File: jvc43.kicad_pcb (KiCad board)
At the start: 6 copper layers, 101.6 x 50.8 mm, 119 parts, among them J201 8P8C_LED_Shielded, J301 8P8C_LED_Shielded, J401 USB_C_Receptacle_USB2.0, U201 LAN8810, U301 LAN8810, U401 LTC3622*DE

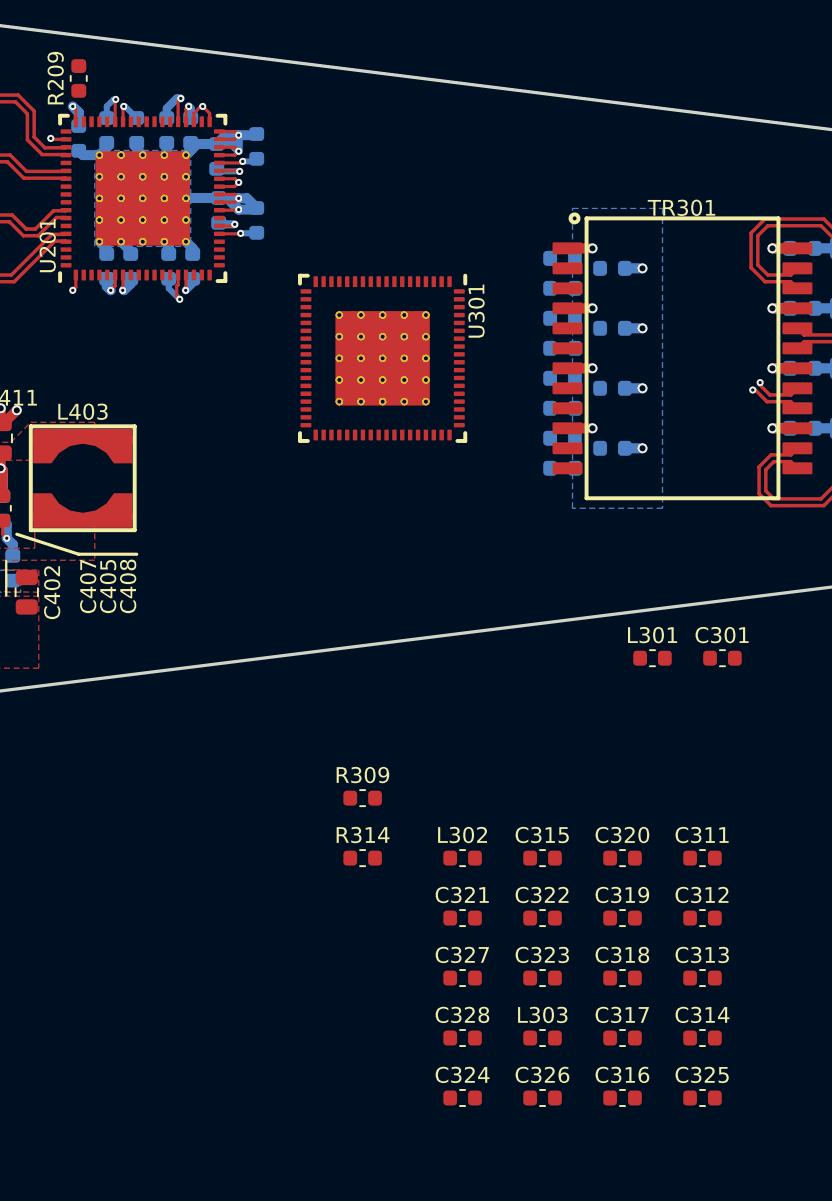
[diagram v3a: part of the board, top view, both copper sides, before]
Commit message: Routed 3/4 of the PHY2 decoupling caps, plus the PHY1-to-PHY2 data lines (but not yet the enables/clock).  Had to alter some traces and clearances down from 8 mils to 7 mils to get a couple things to fit.
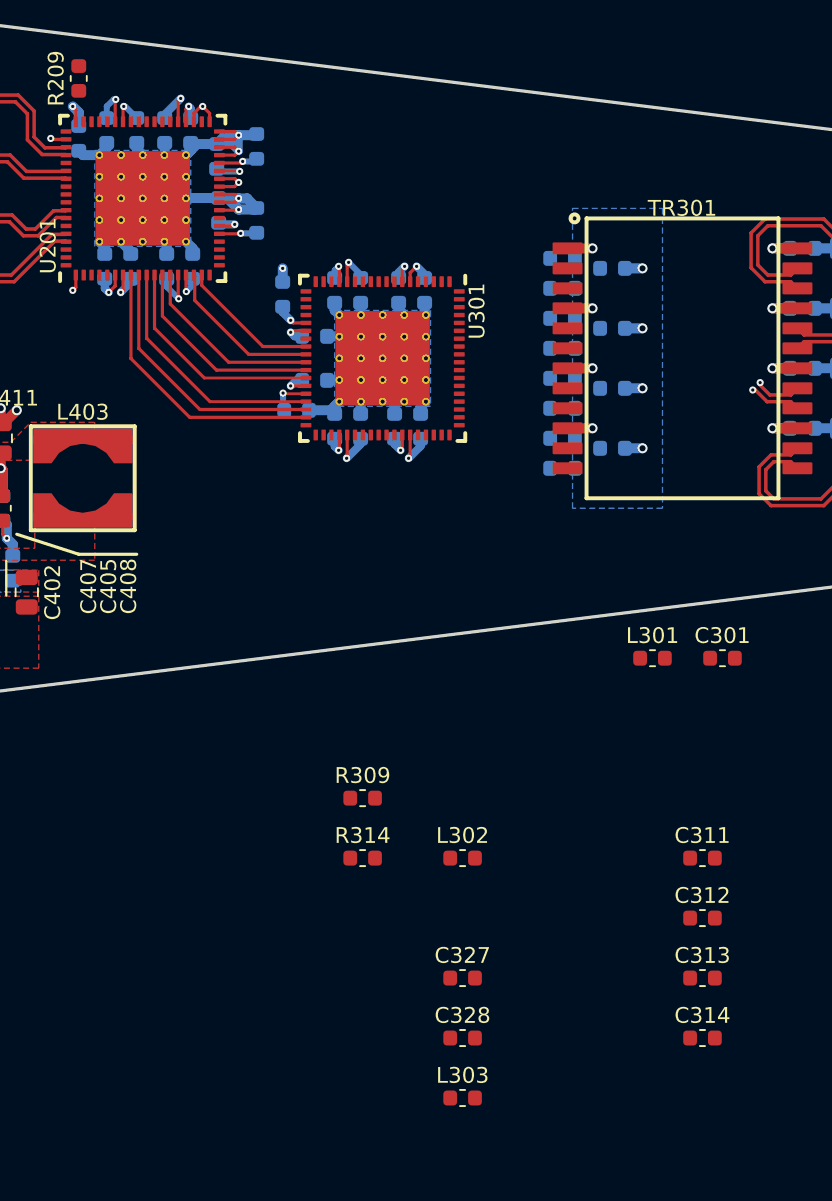
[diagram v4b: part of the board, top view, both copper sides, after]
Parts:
- C315, C316, C317, C318, C319, C320, C321, C322, C323, C324, C325, C326: moved to B.Cu
- moved C316 53.9 mm to (82.4, 46.5), turned to 270 degrees
- moved C317 51.9 mm to (77.5, 46.7), turned to 90 degrees
- moved C325 48.7 mm to (80.8, 55.1), turned to 90 degrees
- moved C324 46.6 mm to (79.5, 52.2)
- moved C326 43.7 mm to (84.6, 55.1), turned to 90 degrees
- moved C323 43.3 mm to (79.5, 49.4)
- moved C322 42.0 mm to (80.8, 46.5), turned to 270 degrees
- moved C318 41.6 mm to (78.4, 54.1)
- moved C321 40.1 mm to (84.8, 46.5), turned to 270 degrees
- moved C315 36.8 mm to (86.5, 46.5), turned to 270 degrees
- moved C319 35.4 mm to (82.4, 55.1), turned to 90 degrees
- moved C320 30.3 mm to (86.2, 55.1), turned to 90 degrees
- moved L303 6.35 mm to (88.9, 97.8)
- moved C215 0.13 mm to (66.2, 45.0)
- moved C216 0.13 mm to (70.1, 45.0)
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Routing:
- net /Ethernet1/RXD0: track 0.00 -> 18.0 mm
- net /Ethernet1/RXD1: track 0.00 -> 16.9 mm
- net /Ethernet1/RXD2: track 0.00 -> 15.8 mm
- net +2V5: track 22.2 -> 37.8 mm, vias 8 -> 14
- net /Ethernet1/RXD3: track 0.00 -> 14.3 mm
- net /Ethernet1/RXD4: track 0.00 -> 13.1 mm
- net /Ethernet1/RXD5: track 0.00 -> 12.0 mm
- net +1V2: track 24.2 -> 36.0 mm, vias 9 -> 15
- net GND: track 76.8 -> 88.0 mm, vias 35 -> 36
- net /Ethernet1/RXD6: track 0.00 -> 10.1 mm
- net /Ethernet1/RXD7: track 0.00 -> 8.89 mm
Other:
- net class CloseSig removed
- net class UghClear added: clearance 0.1778, trace_width 0.1778, via_dia 0.4572, via_drill 0.2032
- rule trace_min: 0.2032 -> 0.1778

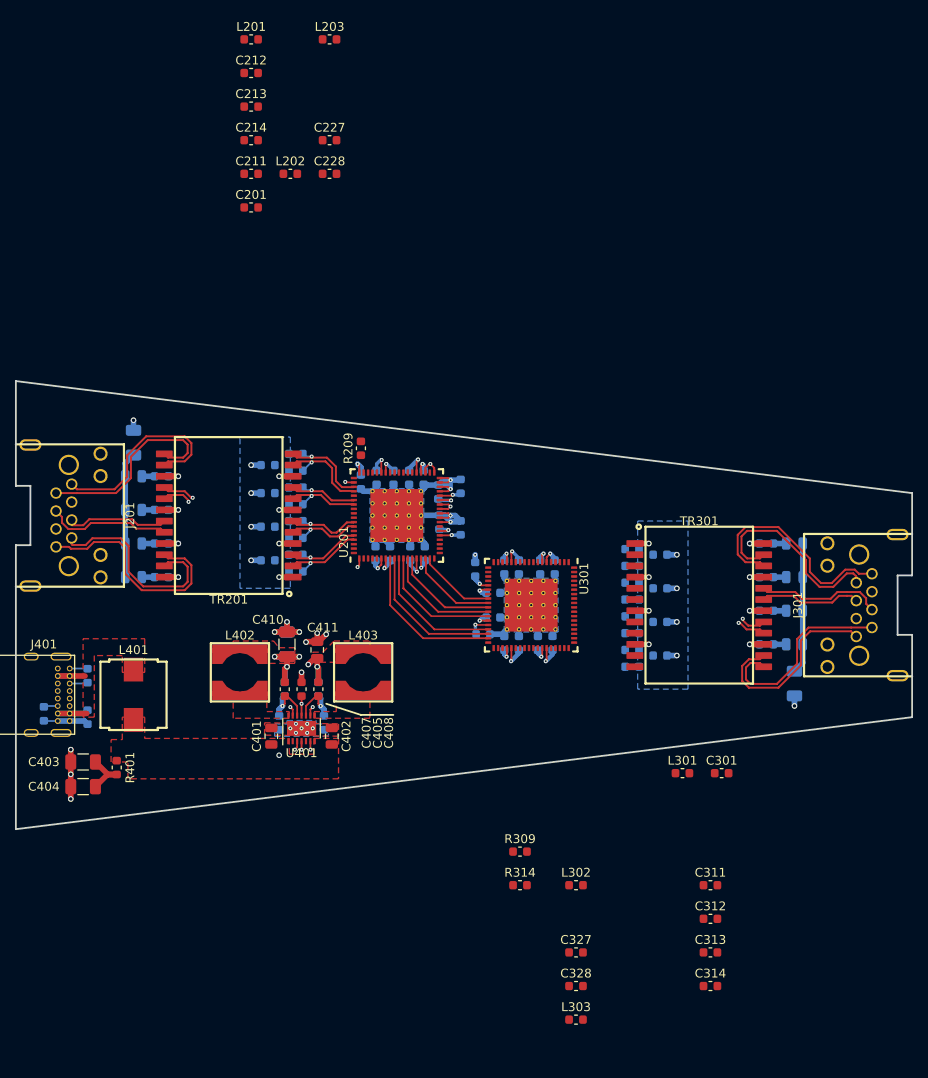
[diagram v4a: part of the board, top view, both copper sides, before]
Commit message: - Routed the PHY2-to-magnetics diff pairs - Routed all the remaining PHY2 decoupling caps, and even the chip inductors,   except for the VDD_ETH one - Spent some time swizzling rear silkscreen labels to look nice - Moved PHY1 eth_bias resistor from bottom to top, to match PHY2, and hooked   up PHY1 MDIO terminator resistor
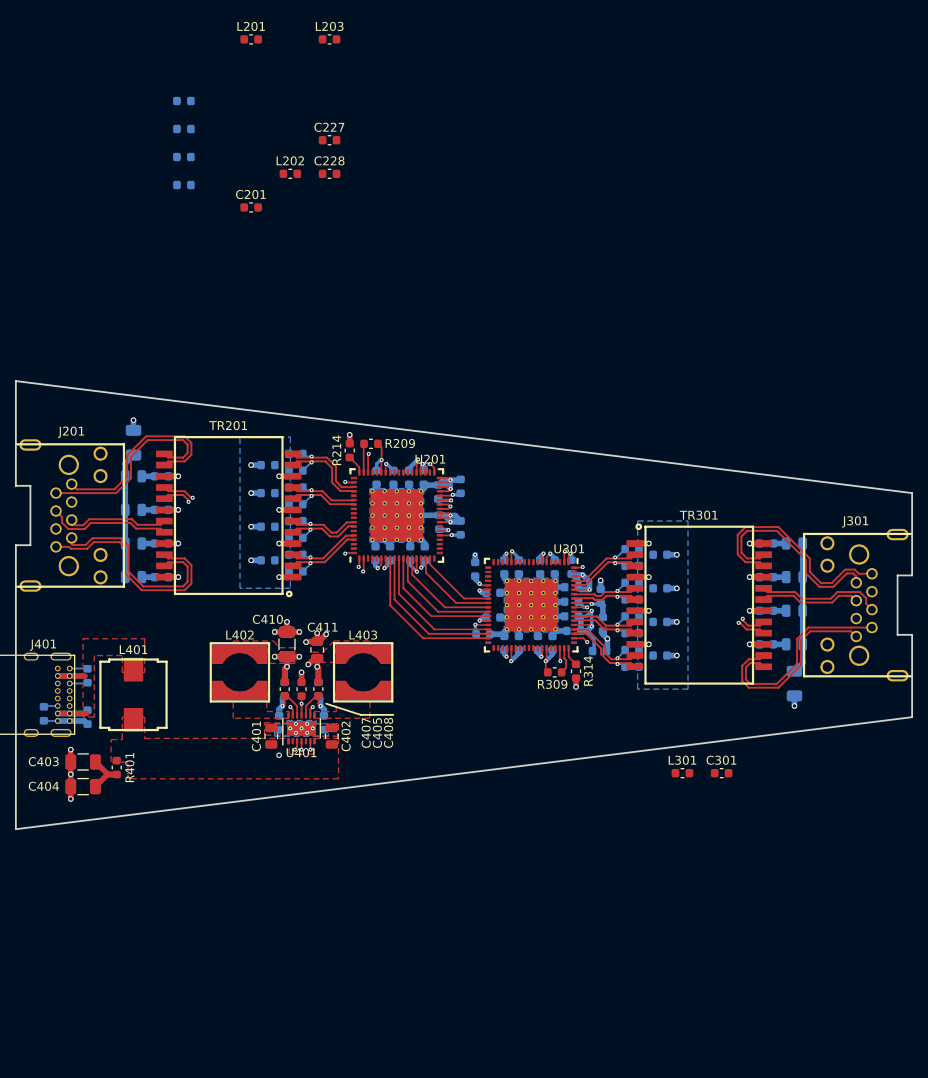
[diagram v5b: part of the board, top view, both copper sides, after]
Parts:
- C211, C212, C213, C214, C311, C312, C313, C314, C327, C328, L302, L303: moved to B.Cu
- R214: moved to F.Cu
- moved C314 50.0 mm to (88.4, 46.5), turned to 90 degrees
- moved L303 44.9 mm to (91.9, 53.0), turned to 90 degrees
- moved C313 44.3 mm to (88.4, 48.8), turned to 180 degrees
- moved C328 44.3 mm to (91.7, 49.8), turned to 90 degrees
- moved C327 39.8 mm to (88.4, 50.4), turned to 180 degrees
- moved C312 37.7 mm to (88.4, 52.1), turned to 180 degrees
- moved C311 32.7 mm to (88.6, 53.7), turned to 180 degrees
- moved L302 26.7 mm to (91.6, 56.0), turned to 180 degrees
- moved R314 25.1 mm to (88.9, 58.3), turned to 270 degrees
- moved R309 20.7 mm to (86.5, 58.4), turned to 180 degrees
- moved C211 11.2 mm to (44.5, -6.35)
- moved C212 9.92 mm to (44.5, -3.17)
- moved C213 9.52 mm to (44.5, 0.00)
- moved C214 9.16 mm to (44.5, 3.17)
- moved R214 3.78 mm to (63.2, 33.3), turned to 90 degrees
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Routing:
- net /Ethernet2/VDD12A: track 0.00 -> 22.8 mm, vias 0 -> 4
- net GND: track 88.0 -> 101.2 mm, vias 36 -> 43
- net /Ethernet2/ETH_TR0+: track 0.00 -> 10.2 mm, vias 0 -> 1
- net /Ethernet2/ETH_TR0-: track 0.00 -> 9.91 mm, vias 0 -> 1
- net /Ethernet2/ETH_TR3+: track 0.00 -> 9.74 mm, vias 0 -> 1
- net /Ethernet2/ETH_TR3-: track 0.00 -> 9.47 mm, vias 0 -> 1
- net /Ethernet2/ETH_TR1+: track 0.00 -> 8.89 mm, vias 0 -> 1
- net /Ethernet2/ETH_TR2+: track 0.00 -> 8.72 mm, vias 0 -> 1
- net /Ethernet2/ETH_TR1-: track 0.00 -> 8.58 mm, vias 0 -> 1
- net /Ethernet2/ETH_TR2-: track 0.00 -> 8.41 mm, vias 0 -> 1
- net +2V5: track 37.8 -> 45.9 mm, vias 14 -> 18
- net +1V2: track 36.0 -> 41.2 mm, vias 15 -> 17
- net /Ethernet2/VDD12PLL: track 0.00 -> 4.80 mm, vias 0 -> 1
- net /Ethernet1/MDIO: track 0.08 -> 3.28 mm
- net /Ethernet2/MDIO: track 0.00 -> 3.03 mm
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- added copper zone on L4.Cu, net /Ethernet2/VDD12A

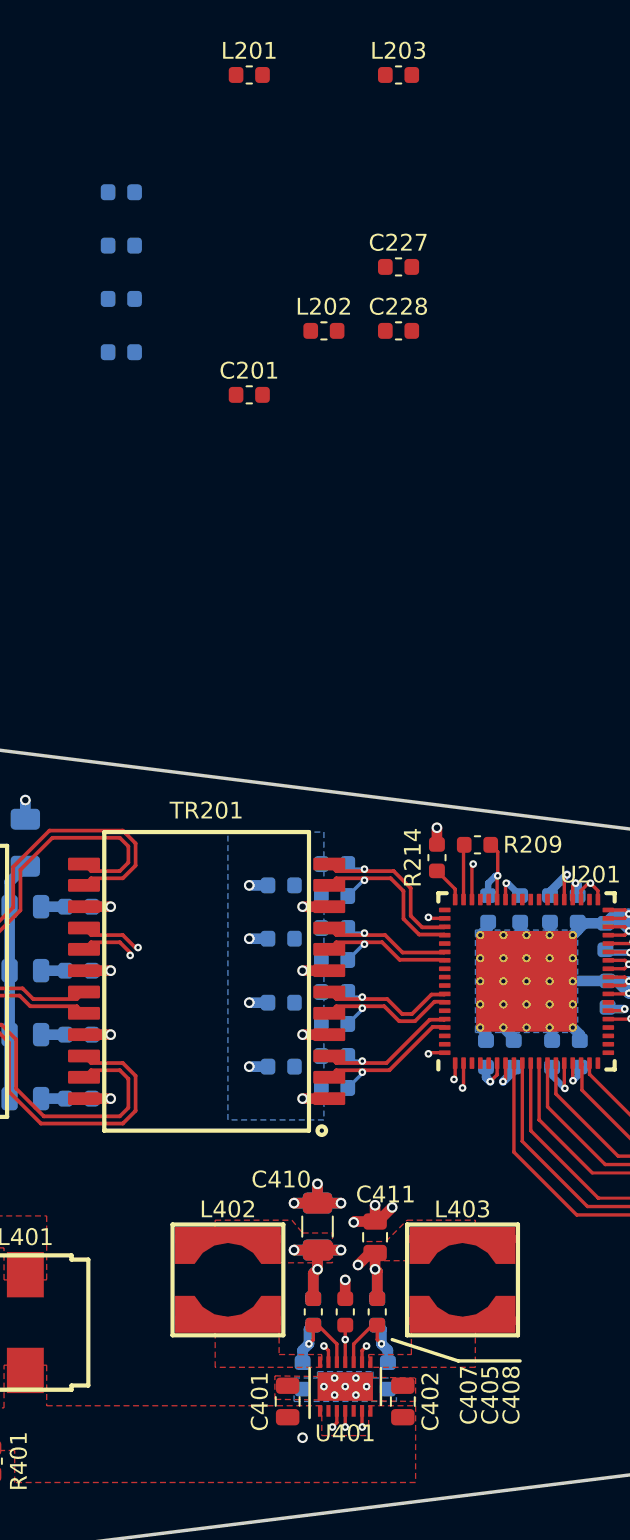
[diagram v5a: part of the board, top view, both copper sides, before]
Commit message: Placed and routed the tricky last 1/4 of bypass caps for PHY1.
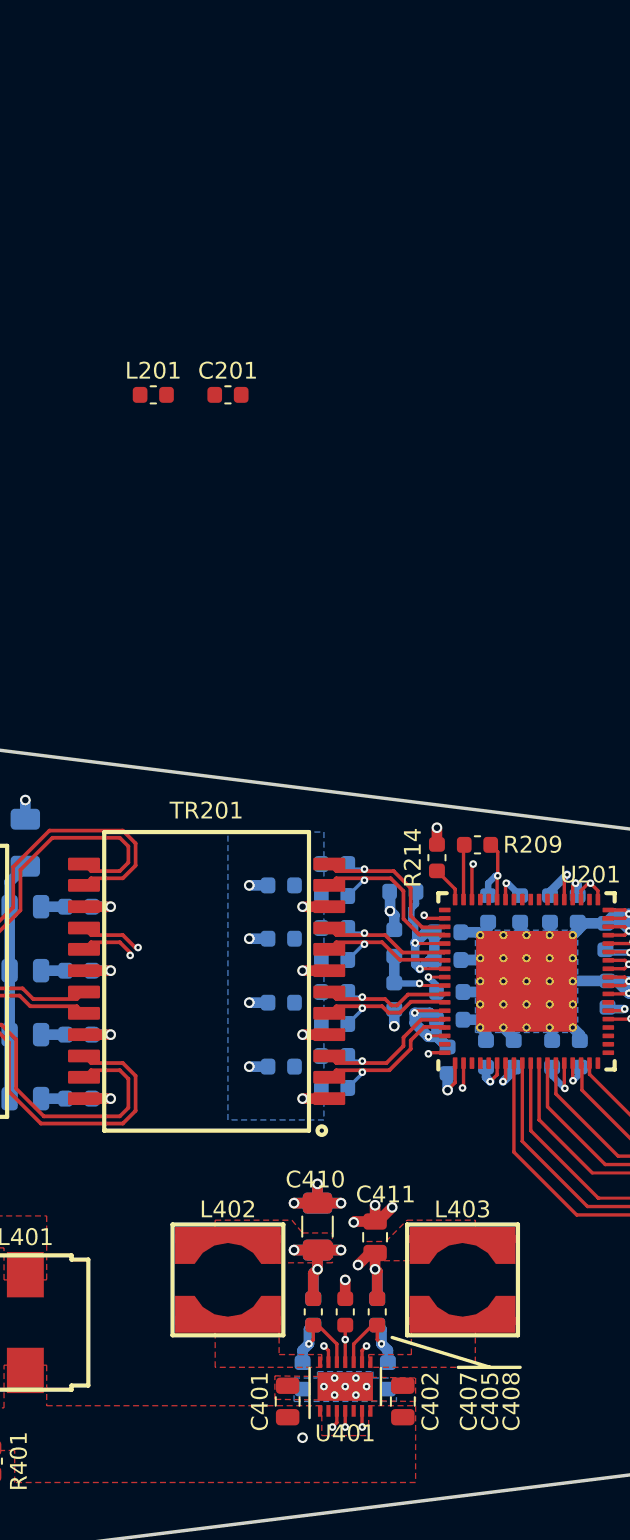
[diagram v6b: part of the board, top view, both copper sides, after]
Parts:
- C227, C228, L202, L203: moved to B.Cu
- moved L203 51.7 mm to (60.7, 38.4), turned to 270 degrees
- moved C211 48.2 mm to (63.9, 37.7)
- moved C213 47.2 mm to (64.0, 42.9)
- moved C212 46.8 mm to (63.9, 39.4)
- moved C214 46.4 mm to (63.9, 45.3), turned to 270 degrees
- moved C227 43.3 mm to (64.0, 41.3)
- moved C228 39.6 mm to (60.7, 41.5), turned to 270 degrees
- moved L202 33.7 mm to (61.2, 35.3)
- moved L201 19.9 mm to (46.4, 5.71)
- moved C201 1.27 mm to (50.8, 5.71)
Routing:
- net /Ethernet1/VDD12A: track 0.00 -> 21.7 mm, vias 0 -> 4
- net GND: track 101.2 -> 108.4 mm, vias 43 -> 44
- net /Ethernet1/VDD12PLL: track 0.00 -> 4.67 mm, vias 0 -> 1
- net +1V2: track 41.2 -> 45.7 mm, vias 17 -> 19
- added copper zone on L4.Cu, net /Ethernet1/VDD12A

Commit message: - Selected, schematic'd, placed & routed a crystal oscillator - Filled various internal planes to even out board thickness as well as   improve EMI performance - Added some identifying text to the top silkscreen
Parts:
- added C101: 10n, Capacitor_SMD:C_0603_1608Metric, F.Cu at (62.0, 50.2)
- added X101: 25 MHz, Crystal:Crystal_SMD_2520-4Pin_2.5x2.0mm, F.Cu at (64.8, 50.2)
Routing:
- net GND: track 108.4 -> 113.1 mm, vias 44 -> 48
- net /Ethernet1/XI: track 0.00 -> 4.03 mm
- net +2V5: track 45.9 -> 49.0 mm, vias 18 -> 19
- added copper zone on L4.Cu, net +2V5
- added copper zone on L5.Cu, net /Ethernet1/gnd_eth
- added copper zone on L5.Cu, net /Ethernet2/gnd_eth
- added copper zone on L5.Cu, net GND
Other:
- board text added: "GigaDiode JVC43A"
- board text added: "Licensed under TAPR OHL v1.0"
- board text added: "©2022 OT Collective"

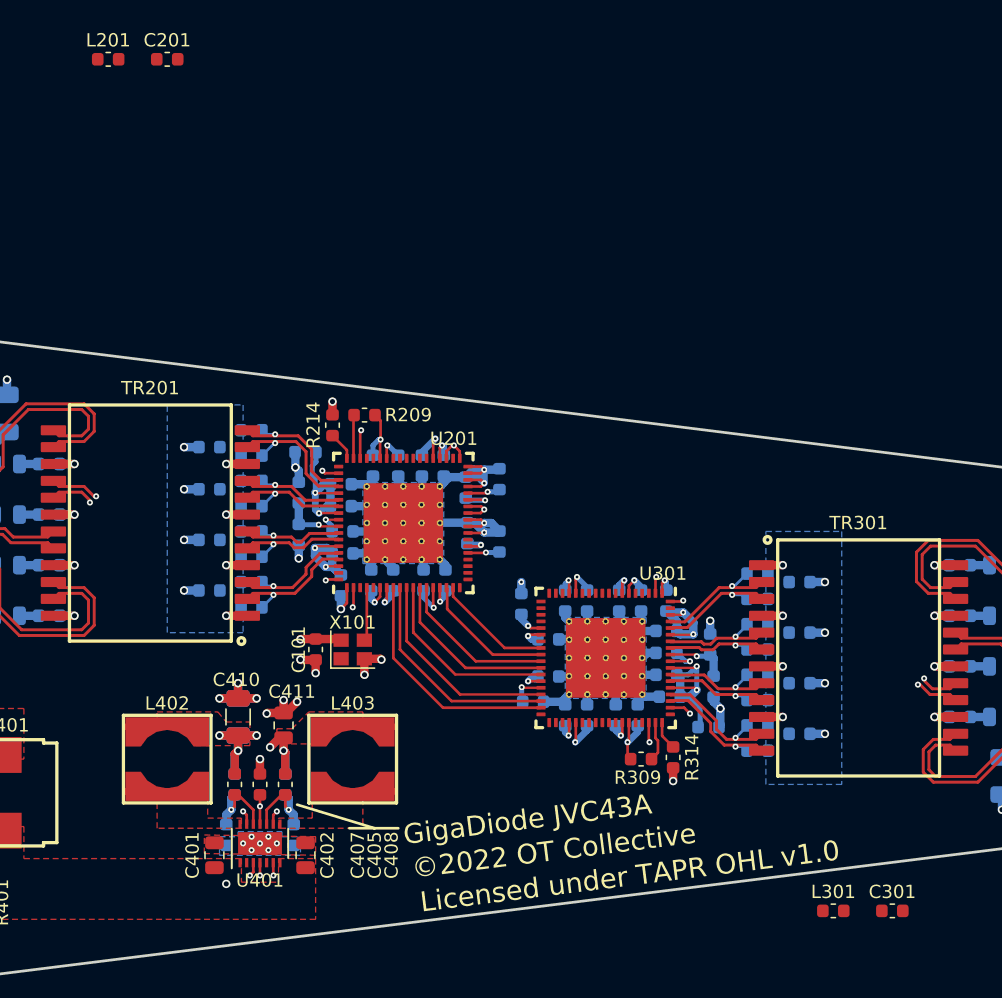
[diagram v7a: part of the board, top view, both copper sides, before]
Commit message: - Removed C201/C301 which were the first two bypass caps on VCC_ETH - Placed last two components - Tweaked some planes, I think? - Finished routing all nets from the current schematic!!!
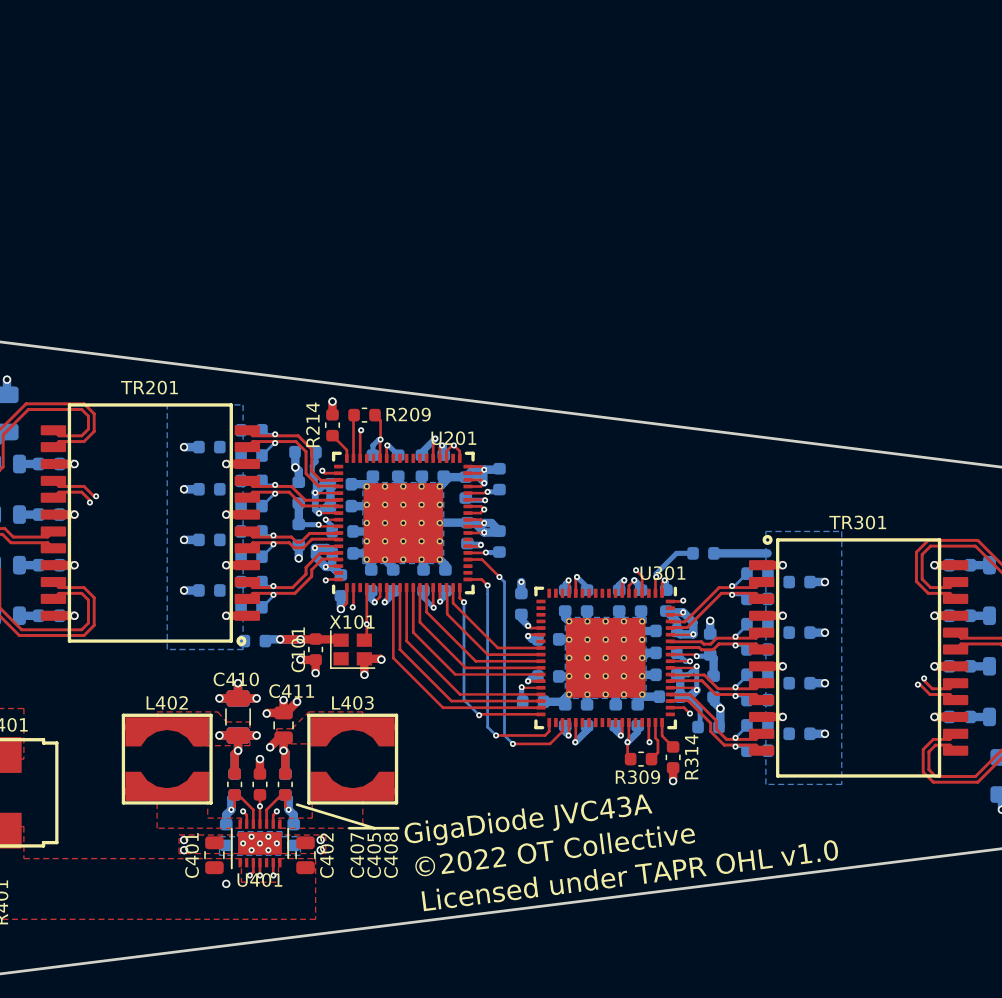
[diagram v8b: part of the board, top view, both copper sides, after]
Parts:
- removed C201, C301: 10n, Capacitor_SMD:C_0603_1608Metric
- L201, L301: moved to B.Cu
- moved L201 45.2 mm to (57.4, 49.5), turned to 180 degrees
- moved L301 28.6 mm to (91.2, 42.9)
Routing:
- net /Ethernet1/XI: track 4.03 -> 28.1 mm, vias 0 -> 2
- net /CLK_W2B: track 0.00 -> 20.7 mm, vias 0 -> 2
- net /ER_W2B: track 0.00 -> 18.0 mm, vias 0 -> 2
- net /EN_W2B: track 0.00 -> 14.9 mm, vias 0 -> 2
- net +2V5: track 49.0 -> 56.9 mm, vias 19 -> 20
- net /Ethernet2/VDD_ETH: track 6.35 -> 10.4 mm
- net GND: vias 48 -> 52
